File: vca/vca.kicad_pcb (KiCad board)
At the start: 2 copper layers, 69.6 x 99.6 mm, 25 parts, among them J1 Conn_01x03_Socket, J2 Conn_01x02_Socket, J3 Conn_01x02_Socket, J4 Conn_01x02_Socket, J5 Conn_01x03_Socket, Q1 BC548C, Q2 BC548C, U1 TL074

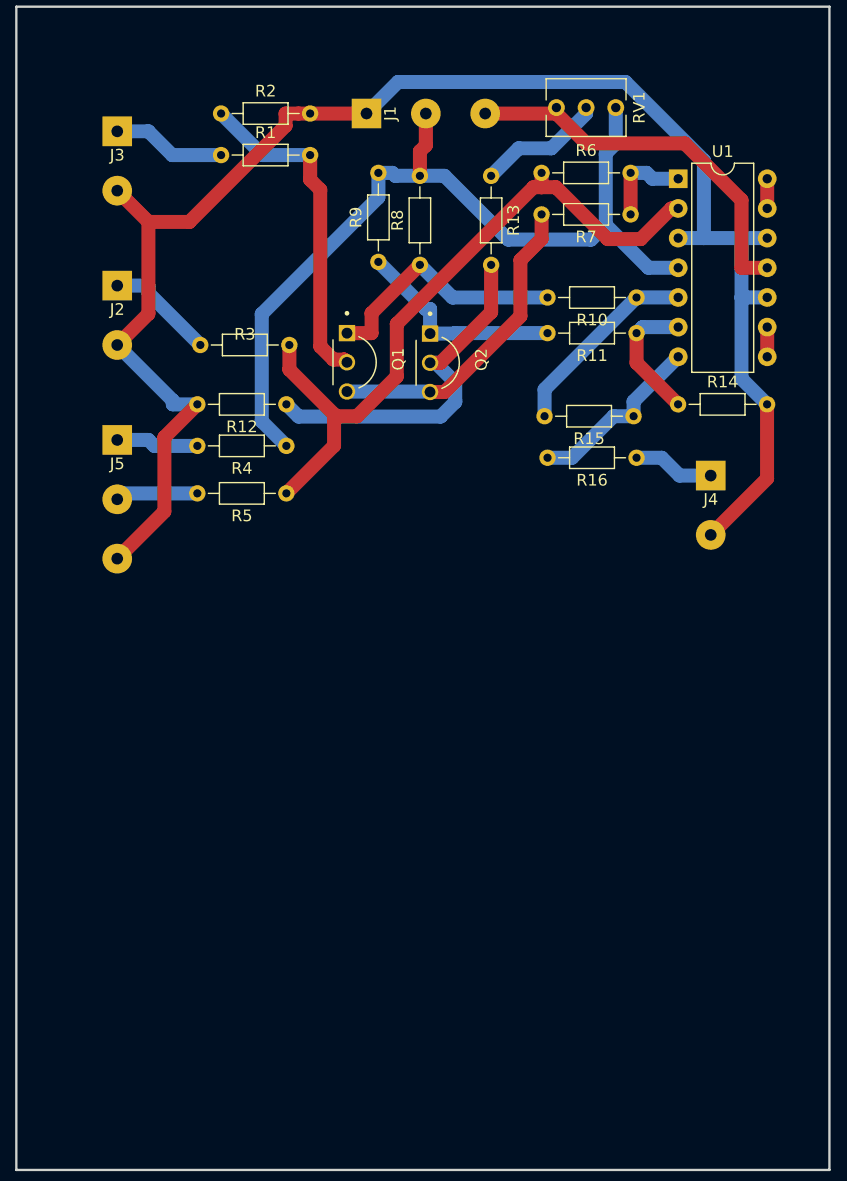
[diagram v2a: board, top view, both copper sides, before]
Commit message: turn vca to dual vca add mounting holes
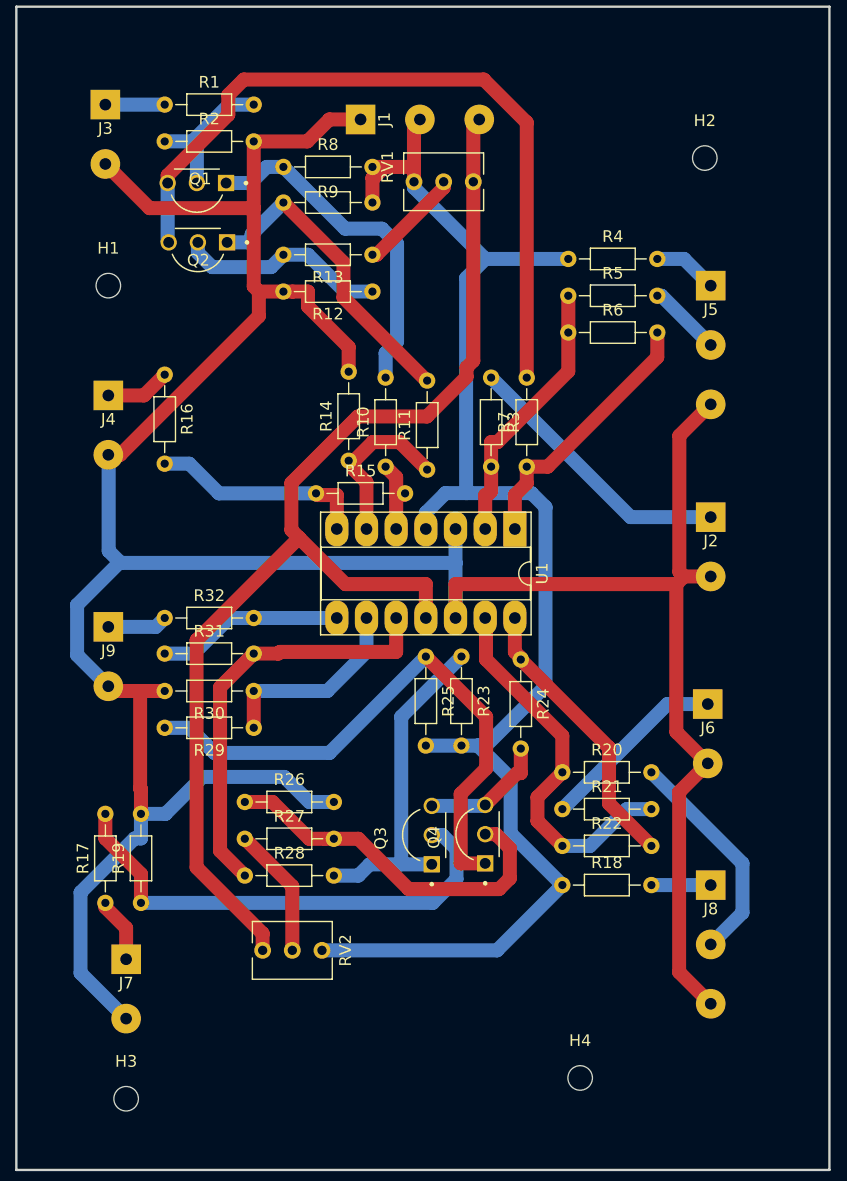
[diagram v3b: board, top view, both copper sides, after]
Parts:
- added H1: MountingHole, MountingHole:MountingHole_2.1mm, F.Cu at (172.0, 75.7)
- added H2: MountingHole, MountingHole:MountingHole_2.1mm, F.Cu at (223.0, 64.8)
- added H3: MountingHole, MountingHole:MountingHole_2.1mm, F.Cu at (173.5, 145.3)
- added H4: MountingHole, MountingHole:MountingHole_2.1mm, F.Cu at (212.3, 143.5)
- added J6: Conn_01x02_Socket, my_library:my_really_cool_2pin, F.Cu at (223.3, 114.0)
- added J7: Conn_01x02_Socket, my_library:my_really_cool_2pin, F.Cu at (173.5, 135.9)
- added J8: Conn_01x03_Socket, my_library:my_really_cool_3pin, F.Cu at (223.5, 129.5)
- added J9: Conn_01x02_Socket, my_library:my_really_cool_2pin, F.Cu at (172.0, 107.4)
- added Q3: BC548C, BC548C:TO92250P510H770-3, F.Cu at (199.0, 122.7)
- added Q4: BC548C, BC548C:TO92250P510H770-3, F.Cu at (203.6, 122.6)
- added R17: 100k, Resistor_THT:R_Axial_DIN0204_L3.6mm_D1.6mm_P7.62mm_Horizontal, F.Cu at (171.7, 128.5)
- added R18: 20k, Resistor_THT:R_Axial_DIN0204_L3.6mm_D1.6mm_P7.62mm_Horizontal, F.Cu at (210.8, 127.0)
- added R19: 100, Resistor_THT:R_Axial_DIN0204_L3.6mm_D1.6mm_P7.62mm_Horizontal, F.Cu at (174.8, 128.5)
- added R20: 100k, Resistor_THT:R_Axial_DIN0204_L3.6mm_D1.6mm_P7.62mm_Horizontal, F.Cu at (210.8, 117.3)
- added R21: 100k, Resistor_THT:R_Axial_DIN0204_L3.6mm_D1.6mm_P7.62mm_Horizontal, F.Cu at (210.8, 120.5)
- added R22: 82k, Resistor_THT:R_Axial_DIN0204_L3.6mm_D1.6mm_P7.62mm_Horizontal, F.Cu at (210.8, 123.6)
- added R23: 20k, Resistor_THT:R_Axial_DIN0204_L3.6mm_D1.6mm_P7.62mm_Horizontal, F.Cu at (202.2, 107.4)
- added R24: 10k, Resistor_THT:R_Axial_DIN0204_L3.6mm_D1.6mm_P7.62mm_Horizontal, F.Cu at (207.3, 107.7)
- added R25: 20k, Resistor_THT:R_Axial_DIN0204_L3.6mm_D1.6mm_P7.62mm_Horizontal, F.Cu at (199.1, 107.4)
- added R26: 100, Resistor_THT:R_Axial_DIN0204_L3.6mm_D1.6mm_P7.62mm_Horizontal, F.Cu at (183.6, 119.9)
- added R27: 100k, Resistor_THT:R_Axial_DIN0204_L3.6mm_D1.6mm_P7.62mm_Horizontal, F.Cu at (183.6, 123.0)
- added R28: 10k, Resistor_THT:R_Axial_DIN0204_L3.6mm_D1.6mm_P7.62mm_Horizontal, F.Cu at (183.6, 126.2)
- added R29: 10k, Resistor_THT:R_Axial_DIN0204_L3.6mm_D1.6mm_P7.62mm_Horizontal, F.Cu at (184.4, 113.5)
- added R30: 100k, Resistor_THT:R_Axial_DIN0204_L3.6mm_D1.6mm_P7.62mm_Horizontal, F.Cu at (184.4, 110.4)
- added R31: 100k, Resistor_THT:R_Axial_DIN0204_L3.6mm_D1.6mm_P7.62mm_Horizontal, F.Cu at (176.8, 107.2)
- added R32: 1k, Resistor_THT:R_Axial_DIN0204_L3.6mm_D1.6mm_P7.62mm_Horizontal, F.Cu at (176.8, 104.1)
- added RV2: 100k, Potentiometer_THT:Potentiometer_Vishay_T73XW_Horizontal, F.Cu at (190.2, 132.6)
- U1: footprint Package_DIP:DIP-14_W7.62mm -> my_library:my_dip14
- moved J2 54.5 mm to (223.5, 98.0)
- moved J5 52.5 mm to (223.5, 78.2)
- moved J4 52.0 mm to (172.0, 87.6)
- moved R16 41.0 mm to (176.8, 83.3), turned to -90 degrees
- moved U1 33.1 mm to (206.8, 96.5), turned to -90 degrees
- moved R5 29.5 mm to (211.3, 76.6), turned to 0 degrees
- moved R4 29.0 mm to (211.3, 73.4), turned to 0 degrees
- moved R14 28.6 mm to (192.5, 90.7), turned to 90 degrees
- moved R15 28.0 mm to (189.7, 93.5), turned to 0 degrees
- moved R10 25.9 mm to (195.7, 91.2), turned to 90 degrees
- moved R3 25.0 mm to (204.7, 83.6), turned to -90 degrees
- moved R7 23.3 mm to (207.8, 91.2), turned to 90 degrees
- moved Q2 22.7 mm to (179.6, 72.6), turned to 180 degrees
- moved R11 21.4 mm to (199.2, 91.4), turned to 90 degrees
- moved Q1 20.0 mm to (179.5, 67.6), turned to 180 degrees
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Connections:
- U1 pad 10: GND -> Net-(U1C-+)
- U1 pad 14: Net-(U1D--) -> Net-(R22-Pad2)
- U1 pad 8: Net-(U1C--) -> Net-(R31-Pad1)
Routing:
- net GND: track 141.3 -> 264.9 mm
- net -12V: track 33.5 -> 102.9 mm
- net +12V: track 74.4 -> 127.9 mm
- net Net-(Q4-Pad1): track 0.00 -> 49.5 mm
- net Net-(Q3-Pad2): track 0.00 -> 41.9 mm
- net Net-(Q1-Pad3): track 27.0 -> 64.3 mm
- net Net-(U1A--): track 60.3 -> 23.3 mm
- net Net-(U1C-+): track 0.00 -> 36.2 mm
- net Net-(Q4-Pad2): track 0.00 -> 31.3 mm
- net Net-(U1D--): track 2.54 -> 32.9 mm
- net Net-(Q3-Pad1): track 0.00 -> 28.7 mm
- net Net-(R22-Pad2): track 0.00 -> 24.3 mm
- net Net-(J8-Pin_2): track 0.00 -> 19.1 mm
- net Net-(J6-Pin_1): track 0.00 -> 16.2 mm
- net Net-(Q1-Pad2): track 28.7 -> 12.6 mm
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
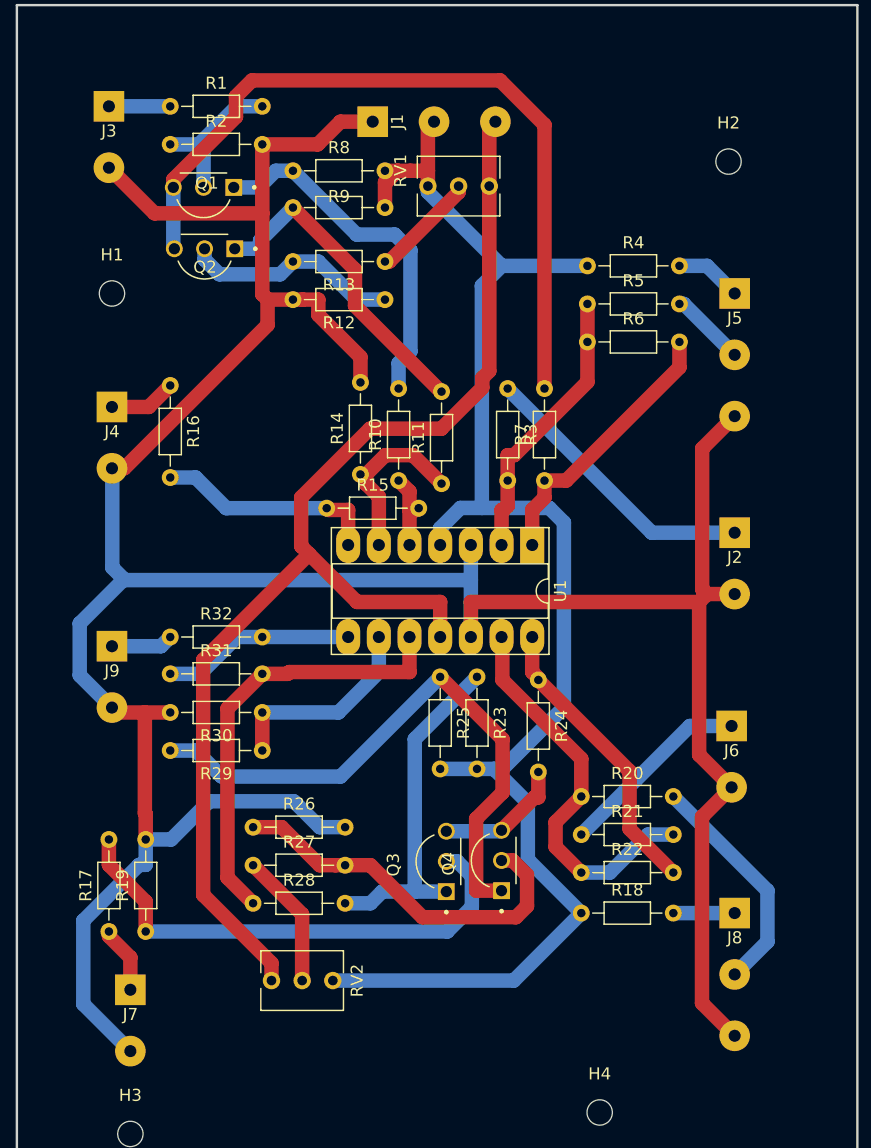
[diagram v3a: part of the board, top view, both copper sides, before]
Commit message: use custom footprints with bigger pads
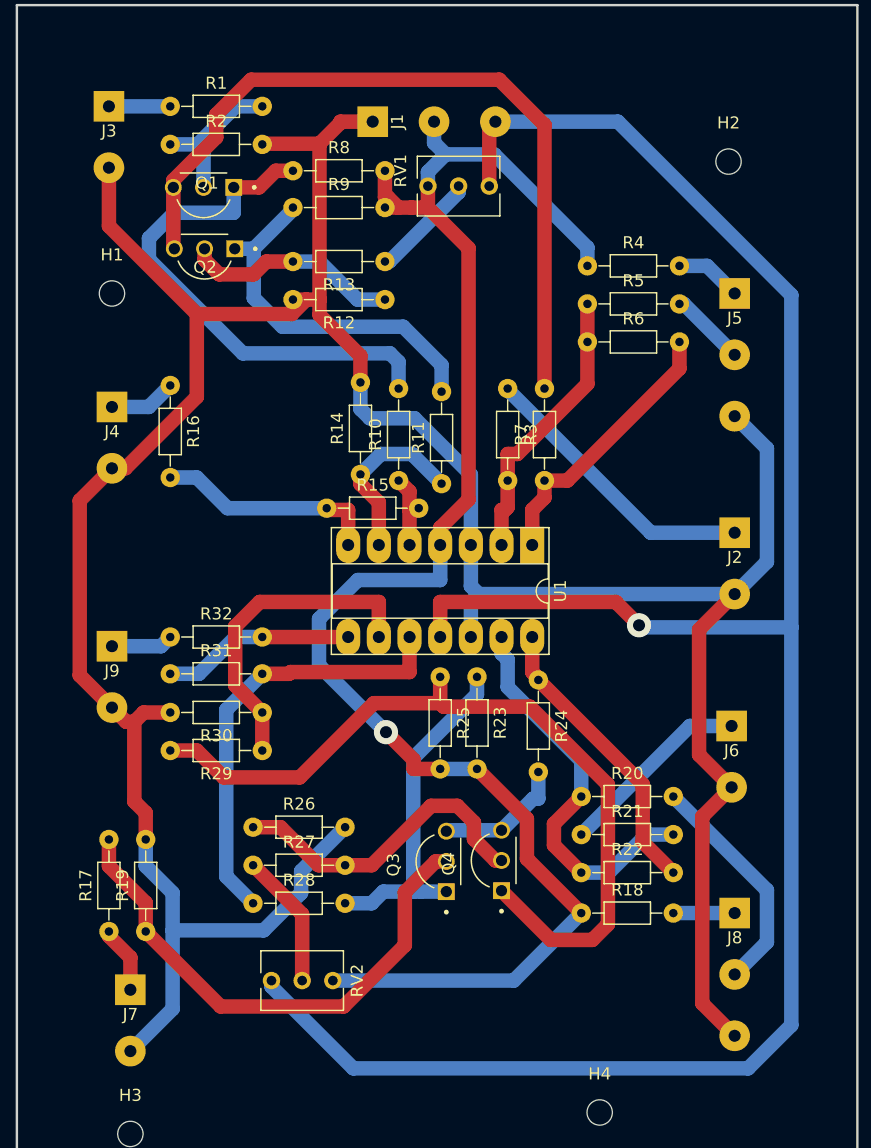
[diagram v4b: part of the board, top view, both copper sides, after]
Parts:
- R1, R10, R11, R12, R13, R14, R15, R16, R17, R18, R19, R2, R20, R21, R22, R23, R24, R25, R26, R27, R28, R29, R3, R30, R31, R32, R4, R5, R6, R7, R8, R9: footprint Resistor_THT:R_Axial_DIN0204_L3.6mm_D1.6mm_P7.62mm_Horizontal -> my_library:my_tht_r
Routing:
- net -12V: track 102.9 -> 177.1 mm, vias 0 -> 1
- net Net-(Q4-Pad1): track 49.5 -> 67.3 mm
- net Net-(Q1-Pad1): track 29.8 -> 43.6 mm
- net Net-(U1C--): track 17.1 -> 26.8 mm
- net +12V: track 127.9 -> 135.7 mm, vias 0 -> 1
- net GND: track 264.9 -> 257.7 mm
- net Net-(Q4-Pad2): track 31.3 -> 26.6 mm
- net Net-(Q2-Pad1): track 27.0 -> 30.5 mm
- net Net-(Q3-Pad2): track 41.9 -> 43.9 mm

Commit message: update almost all other footprints to fatty pads
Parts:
- Q1, Q2, Q3, Q4: footprint BC548C:TO92250P510H770-3 -> my_library:my_bc548
- RV1, RV2: footprint Potentiometer_THT:Potentiometer_Vishay_T73XW_Horizontal -> my_library:my_trimmer
- moved Q3 4.95 mm to (201.7, 126.9), turned to 0 degrees
- moved Q4 4.44 mm to (201.7, 118.6), turned to 0 degrees
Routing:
- net Net-(Q4-Pad1): track 67.3 -> 34.7 mm
- net Net-(Q1-Pad1): track 43.6 -> 74.1 mm
- net Net-(U1C-+): track 36.3 -> 64.8 mm
- net Net-(Q1-Pad3): track 64.4 -> 42.3 mm
- net Net-(U1C--): track 26.8 -> 17.1 mm
- net +12V: track 135.7 -> 127.2 mm, vias 1 -> 0
- net GND: track 257.7 -> 250.8 mm
- net Net-(Q3-Pad2): track 43.9 -> 38.1 mm
- net Net-(Q4-Pad2): track 26.6 -> 21.7 mm
- net Net-(Q2-Pad1): track 30.5 -> 26.2 mm
- net Net-(Q3-Pad3): track 10.9 -> 14.3 mm
- net Net-(Q3-Pad1): track 28.7 -> 31.7 mm
- net -12V: track 177.1 -> 175.2 mm, vias 1 -> 0

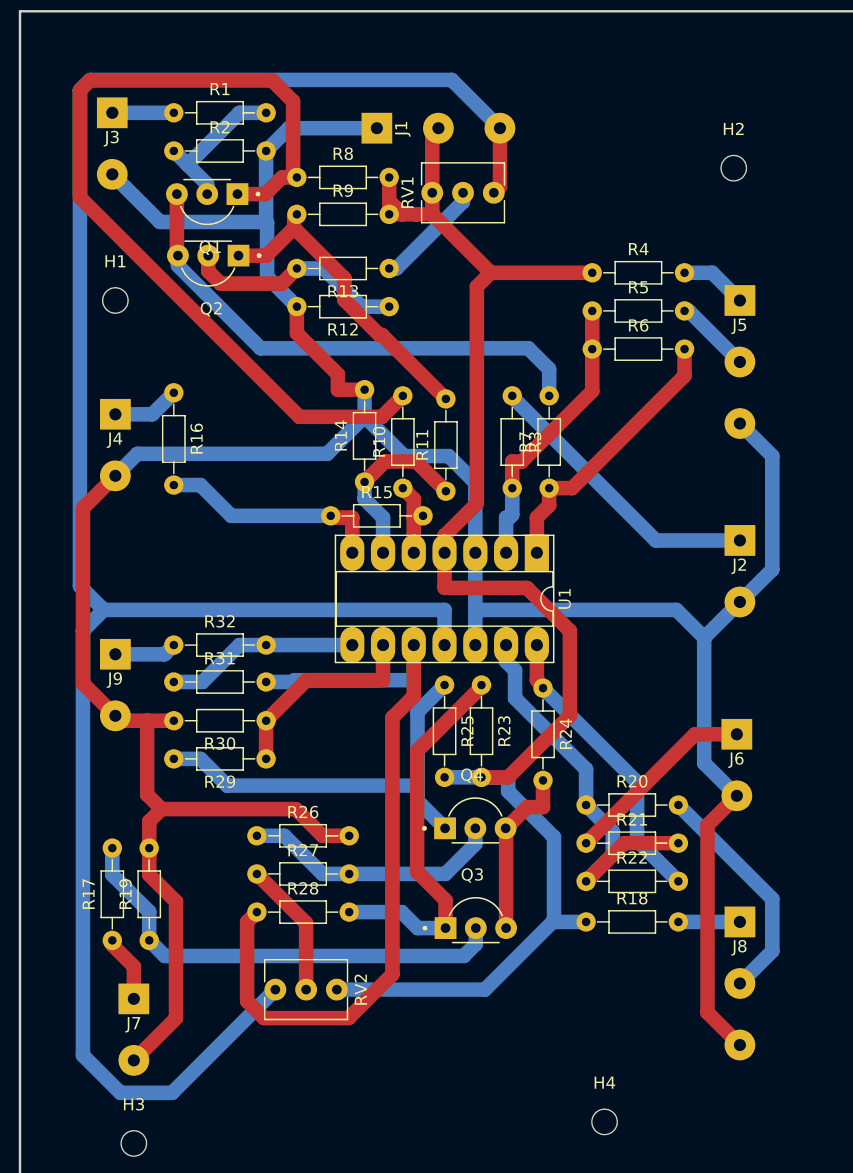
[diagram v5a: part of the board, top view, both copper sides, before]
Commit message: FRIENDSHIP ENDED WITH PACKAGE_DIP. added a keep-out on F.cu for dip14
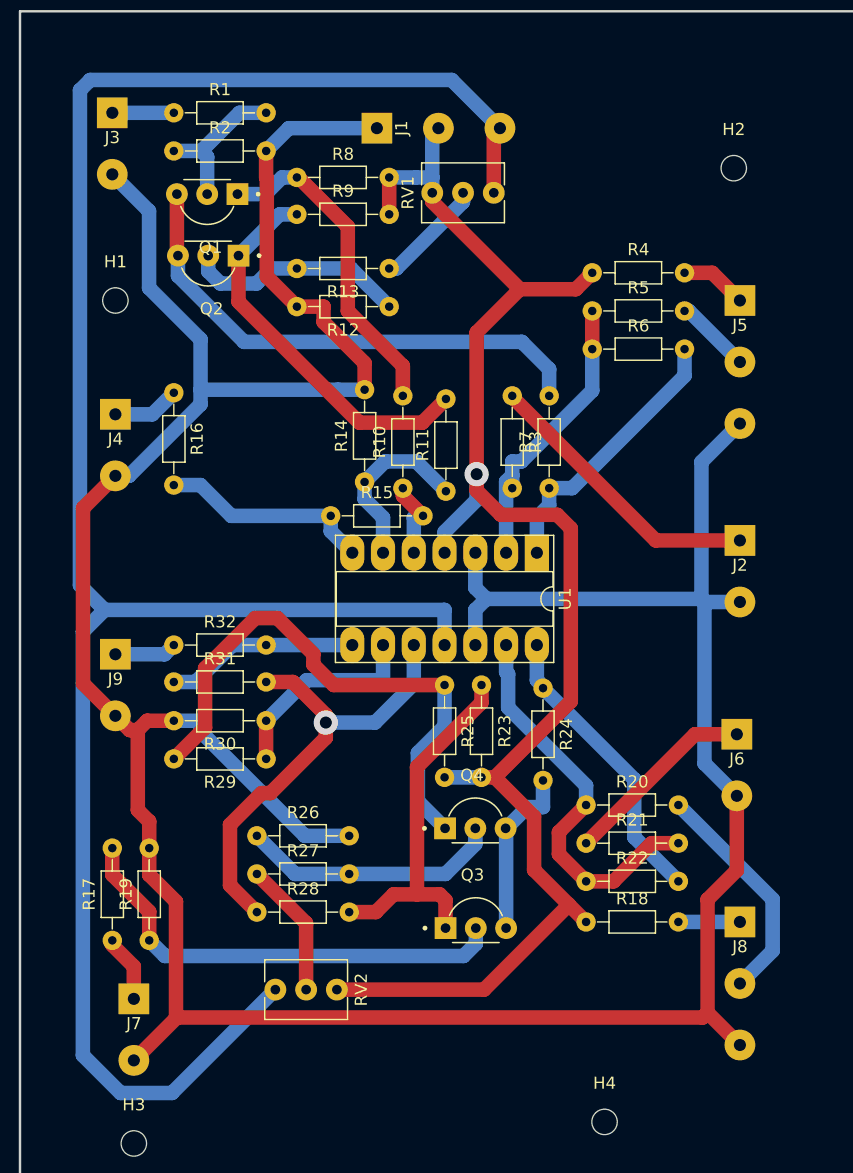
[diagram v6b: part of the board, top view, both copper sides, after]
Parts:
- U1: footprint my_library:my_dip14 -> my_library:my_dip14_no_f_pads
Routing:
- net Net-(Q1-Pad1): track 74.1 -> 27.2 mm
- net GND: track 250.8 -> 285.0 mm
- net Net-(U1C-+): track 64.8 -> 38.7 mm, vias 0 -> 1
- net Net-(Q4-Pad1): track 34.7 -> 46.5 mm
- net Net-(Q2-Pad1): track 26.2 -> 32.1 mm
- net +12V: track 127.2 -> 128.8 mm, vias 0 -> 1
- net Net-(Q3-Pad1): track 31.7 -> 30.5 mm
- net Net-(R15-Pad1): track 18.7 -> 17.8 mm
- net Net-(U1A--): track 23.5 -> 24.4 mm
